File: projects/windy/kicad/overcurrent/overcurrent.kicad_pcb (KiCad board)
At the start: 2 copper layers, 100 x 100 mm, 54 parts, among them J1 USB, J2 USB, J3 USB, J4 USB, K1 VF4_RELAY, P1 SD_CARD, P2 ISP, Q1 PNP, SW1 SWITCHES, U1 ATMEGA328-P, U2 ZXCT1009, U3 LM324, U4 74HC164, U5 DS1307, X1 32k768, Y1 HD44780

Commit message: work in progress
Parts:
- removed the 1PIN at (3.81, 95.9)
- removed the 1PIN at (95.9, 95.9)
- removed the 1PIN at (96.5, 3.81)
- removed the 1PIN at (3.81, 3.81)
- removed J3, J4: USB, conn:USB_A
- removed Y1: HD44780, custom:HD44780
- added 1PIN: P***, conn:1pin, F.Cu at (34.3, 181.6)
- added 1PIN: P***, conn:1pin, F.Cu at (76.2, 181.6)
- added 1PIN: P***, conn:1pin, F.Cu at (127.0, 85.0)
- added 1PIN: P***, conn:1pin, F.Cu at (34.3, 85.0)
- added C7: 0.1u, custom:SM0603_VALUE, F.Cu at (94.2, 185.0)
- added C8: 0.1u, custom:SM0603_VALUE, F.Cu at (90.5, 176.3)
- added D2: DIODE, custom:SOD-323_DIODE, F.Cu at (93.8, 180.0)
- added DS1: HD44780, custom:HD44780, B.Cu at (71.1, 121.9)
- added K2: RELAY_OMRON_G5LE-1, mod:OMNRON G5LE, F.Cu at (71.1, 154.9)
- added Q2: PNP, SMD_Packages:SOT-323, F.Cu at (95.0, 189.1)
- added R17, R18, R19: 51k, custom:SM0603_VALUE, F.Cu at (90.5, 176.3)
- added R20: 1k, custom:SM0603_VALUE, F.Cu at (90.5, 176.3)
- added TB5: 12V, Connect:BARREL_JACK, F.Cu at (41.9, 184.2)
- added TB6: 12V, Connect:BARREL_JACK, F.Cu at (53.3, 184.2)
- C1, C2, C3, C4, C5, R1, R10, R11, R12, R13, R14, R2, R3, R4, R6, R7, R8, R9: footprint cms:SM0805 -> custom:SM0603_VALUE
- C6: value .1u -> 0.1u; footprint cms:SM0805 -> custom:SM0603_VALUE
- D1: footprint discrete:D3 -> custom:SOD-323_DIODE
- K1: value VF4_RELAY -> RELAY_OMRON_G5LE-1; footprint custom:VF4_SOCKET -> mod:OMNRON G5LE
- P1: footprint custom:SD_MMC -> custom:475710001
- Q1: footprint cms:SOT23 -> SMD_Packages:SOT-323
- R15, R16: value 100 -> 51k; footprint cms:SM0805 -> custom:SM0603_VALUE
- SW1: footprint custom:JS5208 -> custom:skrhaae010; moved to B.Cu
- TB1, TB2: footprint custom:TB_2 -> custom:SCREW_TERMINAL_2
- TB3: footprint custom:TB_3 -> custom:SCREW_TERMINAL_3
- U1: moved to B.Cu
- U4: value 74HC164 -> 74LS125
- X1: footprint discrete:QMONTRE -> Crystals_Oscillators_SMD:crystal_FA238-TSX3225
- moved R13 124.3 mm to (114.3, 167.6)
- moved U1 120.7 mm to (71.1, 163.8)
- moved R14 119.4 mm to (114.3, 180.3)
- moved J1 117.9 mm to (114.3, 160.0)
- moved J2 113.7 mm to (113.0, 176.5)
- moved SW1 104.0 mm to (52.1, 163.8), turned to 315 degrees
- moved TB1 98.0 mm to (33.0, 147.3), turned to 270 degrees
- moved K1 97.1 mm to (52.1, 154.9)
- moved TB2 96.8 mm to (33.0, 157.5), turned to 270 degrees
- moved R15 94.6 mm to (90.5, 176.3)
- moved TB3 93.2 mm to (33.0, 170.2), turned to 270 degrees
- moved TB4 92.5 mm to (83.8, 146.1)
- moved R5 90.4 mm to (40.6, 146.1)
- moved BR1 90.4 mm to (40.6, 162.6)
- moved R16 90.4 mm to (90.5, 176.3)
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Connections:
- net /RELAY renamed Net-(Q1-Pad2)
- C6 pad 1: GND -> VCC
- C6 pad 2: VCC -> GND
- J1 pad 1: VCC -> Net-(J1-Pad1)
- J2 pad 1: VCC -> Net-(J1-Pad1)
- P1 pad 2: /SD_CS -> Net-(P1-Pad2)
- P1 pad 5: /SCK -> Net-(P1-Pad5)
- P1 pad 7: /MISO -> Net-(P1-Pad7)
- P2 pad 2: /SCK -> /SCLK
- Q1 pad 1: Net-(Q1-Pad1) -> VCC
- R15 pad 1: Net-(J3-Pad2) -> /SW_L
- R15 pad 2: Net-(J3-Pad3) -> /SW_C
- R16 pad 1: Net-(J4-Pad2) -> /SW_C
- R16 pad 2: Net-(J4-Pad3) -> /SW_U
- RV1 pad 1: GND -> VCC
- RV1 pad 3: VCC -> GND
- SW1 pad 1: GND -> /SW
- U1 pad 10: Net-(U1-Pad10) -> /LCD_BL
- U1 pad 12: /SW_U -> Net-(U1-Pad12)
- U1 pad 13: /SW_D -> Net-(U1-Pad13)
- U1 pad 15: /LCD_E -> Net-(Q2-Pad2)
- U1 pad 19: /SCK -> /SCLK
- U1 pad 2: Net-(U1-Pad2) -> /D4
- U1 pad 21: VCC -> Net-(C8-Pad1)
- U1 pad 26: Net-(U1-Pad26) -> /SW
- U1 pad 3: Net-(U1-Pad3) -> /D5
- U1 pad 4: /SW_C -> /D6
- U1 pad 5: /SW_L -> /D7
- U1 pad 6: /SW_R -> Net-(U1-Pad6)
- U1 pad 9: Net-(U1-Pad9) -> /LCD_E
- U4 pad 1: /MOSI -> GND
- U4 pad 10: Net-(U4-Pad10) -> GND
- U4 pad 11: Net-(U4-Pad11) -> (no net)
- U4 pad 12: Net-(U4-Pad12) -> (no net)
- U4 pad 13: Net-(U4-Pad13) -> (no net)
- U4 pad 14: Net-(U4-Pad14) -> VCC
- U4 pad 2: /MOSI -> /SD_CS
- U4 pad 3: Net-(U4-Pad3) -> Net-(P1-Pad2)
- U4 pad 4: Net-(U4-Pad4) -> GND
- U4 pad 5: Net-(U4-Pad5) -> /SCLK
- U4 pad 6: Net-(U4-Pad6) -> Net-(P1-Pad5)
- U4 pad 7: Net-(U4-Pad7) -> GND
- U4 pad 8: /SCK -> Net-(P1-Pad7)
- U4 pad 9: GND -> /MISO
- VR2 pad 1: /BATTERY -> Net-(K2-Pad3)
- VR2 pad 3: VCC -> Net-(J1-Pad1)
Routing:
- net GND: track 278.4 -> 0.00 mm
- net VCC: track 138.0 -> 0.00 mm
- net /BATTERY: track 91.7 -> 0.00 mm
- net /MOSI: track 54.1 -> 0.00 mm
- net Net-(DS1-Pad3): track 42.4 -> 0.00 mm
- net /Vsense: track 41.7 -> 0.00 mm
- net /DUMMY: track 30.5 -> 0.00 mm
- net /AC1: track 30.1 -> 0.00 mm
- net Net-(C1-Pad2): track 27.6 -> 0.00 mm
- net Net-(C2-Pad2): track 23.3 -> 0.00 mm
- net /RECT: track 22.9 -> 0.00 mm
- net Net-(R8-Pad2): track 14.2 -> 0.00 mm, vias 2 -> 0
- net Net-(C3-Pad1): track 12.9 -> 0.00 mm
- net /ADcurr: track 12.8 -> 0.00 mm
- net Net-(D1-Pad2): track 12.7 -> 0.00 mm
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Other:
- board size 100 x 100 mm -> 100.5 x 103.8 mm

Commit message: starting work on board design
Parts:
- removed 1PIN (x4): P***, conn:1pin
- removed J2: USB, conn:USB_A
- removed K1, K2: RELAY_OMRON_G5LE-1, mod:OMNRON G5LE
- removed RV2: 100, pin:PIN_ARRAY_3X1
- removed TB6: 12V, Connect:BARREL_JACK
- removed VAL: REF, custom:Open_Source_Hardware_Logo
- removed WJ20: VAL**, custom:WJ20
- added C10: 0.1u, custom:SM0603_VALUE, F.Cu at (64.5, 192.0)
- added C11: .1u, custom:SM0603_VALUE, F.Cu at (72.0, 192.5)
- added C12: 470uF, 35V, Discret:C1V5, F.Cu at (118.0, 190.5)
- added C9: 100uF, 35V, Discret:C1V5, F.Cu at (107.0, 189.5)
- added CON1: USB-MINI-B, Connect:USB_Mini-B, F.Cu at (3.00, 142.0)
- added D10: TVS, Housings_SOT-23_SOT-143_TSOT-6:SOT-23, F.Cu at (78.5, 191.0)
- added D3: IN4007, custom:SM0603_DIODE, F.Cu at (58.5, 190.5)
- added D4: LED, LEDs:LED-5MM, F.Cu at (100.0, 136.0)
- added D5: LED, LEDs:LED-5MM, F.Cu at (108.5, 135.5)
- added D6: TVS, Housings_SOT-23_SOT-143_TSOT-6:SOT-23, F.Cu at (100.0, 196.0)
- added D7: TVS, Housings_SOT-23_SOT-143_TSOT-6:SOT-23, F.Cu at (84.5, 190.5)
- added D8: TVS, Housings_SOT-23_SOT-143_TSOT-6:SOT-23, F.Cu at (92.0, 192.5)
- added D9: TVS, Housings_SOT-23_SOT-143_TSOT-6:SOT-23, F.Cu at (82.5, 201.5)
- added F1: FUSE, Fuse_Holders_and_Fuses:BladeFuse-Mini, F.Cu at (46.0, 159.0)
- added F2: FUSE, Fuse_Holders_and_Fuses:BladeFuse-Mini, F.Cu at (46.0, 165.0)
- added P3: ENCODER, Pin_Headers:Pin_Header_Straight_1x05, F.Cu at (127.0, 165.0)
- added Q3: IRF540N, SMD_Packages:DPAK-2, F.Cu at (66.5, 181.0)
- added R21: 100, custom:SM0603_VALUE, F.Cu at (51.0, 192.0)
- added R22: 1k, custom:SM0603_VALUE, F.Cu at (54.5, 188.5)
- added SW2: HWB, custom:sw_42_32, F.Cu at (91.5, 203.5)
- BR1: value RECTIFIER -> FUS45-0045B
- C2, C3: value 1u -> 0.1u
- C4: value 100n -> .1u
- C6, C8: value 0.1u -> .1u
- C7: value 0.1u -> 100uF, 35V; footprint custom:SM0603_VALUE -> Discret:C1V5
- D1: value DIODE -> LED; footprint custom:SOD-323_DIODE -> LEDs:LED-5MM
- D2: value DIODE -> TVS; footprint custom:SOD-323_DIODE -> Housings_SOT-23_SOT-143_TSOT-6:SOT-23
- P1: value SD_CARD -> ISP; footprint custom:475710001 -> custom:ISP_EDGE
- P2: value ISP -> SD_CARD; footprint custom:ISP -> custom:475710001
- Q1, Q2: value PNP -> IRF540N; footprint SMD_Packages:SOT-323 -> SMD_Packages:DPAK-2
- R1: value 2k -> 20k
- R10, R11: value 10k -> 1k
- R13, R14: value 100 -> 10k
- R15: value 51k -> 0.1Ω 1% 5W; footprint custom:SM0603_VALUE -> custom:RESISTOR_POWER
- R16: value 51k -> 10k 1%
- R17: value 51k -> 20k
- R18: value 51k -> 10k
- R19: value 51k -> 1k
- R2: value 1k -> 10k
- R3: value 2k -> 22
- R4: value 1k -> 22
- R5: value .01 9W -> 10k; footprint discrete:TO220_VERT -> custom:SM0603_VALUE
- R6: value 2k -> 1k
- R7: value 40k -> 1k
- R8: value 40k -> 20k
- RV1: footprint pin:PIN_ARRAY_3X1 -> Potentiometers:Potentiometer_WirePads
- SW1: value SWITCHES -> RESET; footprint custom:skrhaae010 -> custom:sw_42_32; moved to F.Cu
- TB1: value DUMMY -> STATOR; footprint custom:SCREW_TERMINAL_2 -> TerminalBlocks:3.5x3
- TB2: value BATTERY -> PVP; footprint custom:SCREW_TERMINAL_2 -> TerminalBlocks:3.5x2
- TB3: value STATOR -> DUMP; footprint custom:SCREW_TERMINAL_3 -> TerminalBlocks:3.5x2
- TB4: value SPST -> BATTERY; footprint pin:pin_array_3x2 -> TerminalBlocks:3.5x2
- TB5: value 12V -> LOAD; footprint Connect:BARREL_JACK -> TerminalBlocks:3.5x2
- U1: value ATMEGA328-P -> LM324; footprint cms:TQFP32 -> Housings_SSOP:TSSOP-14_4.4x5mm_Pitch0.65mm; moved to F.Cu
- U2: value ZXCT1009 -> ATMEGA32U4-A; footprint cms:SOT23 -> Housings_QFP:TQFP-44_10x10mm_Pitch0.8mm
- U3: value LM324 -> INA169; footprint cms:SO14E -> Housings_SOIC:SOIC-8_3.9x4.9mm_Pitch1.27mm
- U4: footprint cms:SO14E -> Housings_SSOP:TSSOP-14_4.4x5mm_Pitch0.65mm
- U5: footprint cms:SO8E -> Housings_SOIC:SOIC-8_3.9x4.9mm_Pitch1.27mm
- VR1, VR2: footprint discrete:TO220_VERT -> SMD_Packages:DPAK-2
- X1: value 32k768 -> 32.768kHz
- moved U1 69.9 mm to (8.89, 195.6)
- moved R5 65.1 mm to (105.5, 151.5)
- moved TB4 52.8 mm to (34.0, 163.5), turned to 270 degrees
- moved U2 49.8 mm to (3.81, 157.5)
- moved SW1 49.3 mm to (3.81, 174.0), turned to 180 degrees
- moved VR1 45.0 mm to (98.0, 162.0)
- moved VR2 44.3 mm to (92.5, 143.0)
- moved R15 42.0 mm to (55.5, 153.0)
- moved Q2 32.5 mm to (66.5, 173.5), turned to 90 degrees
- moved D1 21.5 mm to (91.0, 135.5)
- moved Q1 21.2 mm to (66.5, 166.0)
- moved C7 17.6 mm to (88.0, 168.5)
- moved BR1 17.1 mm to (40.5, 145.5), turned to 90 degrees
- moved TB5 15.8 mm to (34.0, 170.5), turned to 270 degrees
- moved TB3 13.7 mm to (34.0, 156.5)
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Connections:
- net Net-(J1-Pad1) renamed /REGULATED_LOAD
- net Net-(K2-Pad3) renamed /SWITCHED_LOAD
- BR1 pad 1: /RECT -> /SOURCE
- C2 pad 1: /ADcurr -> GND
- C3 pad 1: Net-(C3-Pad1) -> GND
- C3 pad 2: GND -> Net-(C3-Pad2)
- C4 pad 1: GND -> VCC
- C4 pad 2: Net-(C4-Pad2) -> GND
- C7 pad 1: VCC -> /FILTERED_SOURCE
- C8 pad 1: Net-(C8-Pad1) -> VCC
- D1 pad 1: GND -> Net-(D1-Pad1)
- D2 pad 1: GND -> /SOURCE
- D2 pad 2: Net-(D2-Pad2) -> /FUSED_SOURCE
- P1 pad 1: Net-(P1-Pad1) -> /MOSI
- P1 pad 2: Net-(P1-Pad2) -> /SCLK
- P1 pad 3: /MOSI -> /RESET
- P1 pad 5: Net-(P1-Pad5) -> /MOSI
- P2 pad 1: /MOSI -> Net-(P2-Pad1)
- P2 pad 2: /SCLK -> Net-(P2-Pad2)
- P2 pad 3: /RESET -> /MOSI
- P2 pad 5: /MOSI -> Net-(P2-Pad5)
- Q1 pad 1: VCC -> /SOURCE
- Q1 pad 2: Net-(Q1-Pad2) -> Net-(D1-Pad1)
- Q1 pad 3: Net-(D1-Pad2) -> /DUMP_LOAD
- Q2 pad 1: VCC -> /FILTERED_SOURCE
- Q2 pad 2: Net-(Q2-Pad2) -> Net-(D4-Pad1)
- Q2 pad 3: Net-(D2-Pad2) -> /SWITCHED_SOURCE
- R1 pad 1: /BATTERY -> Net-(C1-Pad2)
- R1 pad 2: /ADbatt -> /AC1
- R10 pad 1: /RESET -> Net-(D4-Pad2)
- R10 pad 2: VCC -> GND
- R11 pad 1: /SCL -> Net-(D4-Pad1)
- R11 pad 2: VCC -> /CHARGE_SW
- R12 pad 1: /SDA -> /SCL
- R13 pad 1: Net-(J1-Pad2) -> /SDA
- R13 pad 2: Net-(J1-Pad3) -> VCC
- R14 pad 1: Net-(J2-Pad2) -> Net-(R14-Pad1)
- R14 pad 2: Net-(J2-Pad3) -> VCC
- R15 pad 1: /SW_L -> /BATTERY
- R15 pad 2: /SW_C -> /SWITCHED_SOURCE
- R16 pad 1: /SW_C -> Net-(R16-Pad1)
- R16 pad 2: /SW_U -> GND
- R17 pad 1: /SW_U -> /BATTERY
- R17 pad 2: /SW_R -> /VBATT
- R18 pad 1: /SW_R -> /VBATT
- R18 pad 2: /SW_D -> GND
- R19 pad 1: /SW_D -> Net-(D5-Pad2)
- R2 pad 1: /ADbatt -> Net-(C1-Pad2)
- R20 pad 1: Net-(DS1-Pad15) -> Net-(D5-Pad1)
- R20 pad 2: /LCD_BL -> /LOAD_SW
- R3 pad 1: Net-(C1-Pad2) -> /D+
- R3 pad 2: /AC1 -> Net-(CON1-Pad3)
- R4 pad 1: Net-(C1-Pad2) -> /D-
- R4 pad 2: GND -> Net-(CON1-Pad2)
- R5 pad 1: /Vsense -> VCC
- R5 pad 2: /RECT -> /RESET
- R6 pad 1: Net-(R6-Pad1) -> Net-(D1-Pad2)
- R7 pad 1: Net-(C2-Pad2) -> Net-(D1-Pad1)
- R7 pad 2: Net-(R6-Pad1) -> /DUMP_SW
- R8 pad 1: Net-(C3-Pad1) -> /FILTERED_SOURCE
- R8 pad 2: Net-(R8-Pad2) -> /VIN
- R9 pad 1: Net-(C4-Pad2) -> /VIN
- R9 pad 2: Net-(Q1-Pad2) -> GND
- SW1 pad 1: /SW -> GND
- SW1 pad 2: /SW_L -> /RESET
- TB1 pad 1: /DUMMY -> /AC1
- TB1 pad 2: GND -> /AC2
- TB2 pad 1: /BATTERY -> GND
- TB2 pad 2: GND -> /SOURCE
- TB3 pad 1: /AC1 -> /DUMP_LOAD
- TB3 pad 2: /AC2 -> GND
- TB4 pad 1: Net-(C4-Pad2) -> /BATTERY
- U1 pad 1: /RESET -> /TACH
- U1 pad 10: /LCD_BL -> (no net)
- U1 pad 11: /TACH -> GND
- U1 pad 12: Net-(U1-Pad12) -> (no net)
- U1 pad 13: Net-(U1-Pad13) -> (no net)
- U1 pad 14: Net-(Q1-Pad2) -> (no net)
- U1 pad 2: /D4 -> GND
- U1 pad 3: /D5 -> Net-(C1-Pad2)
- U1 pad 4: /D6 -> VCC
- U1 pad 5: /D7 -> Net-(R16-Pad1)
- U1 pad 6: Net-(U1-Pad6) -> /CURR
- U1 pad 7: VCC -> /CURR
- U1 pad 8: GND -> (no net)
- U1 pad 9: /LCD_E -> (no net)
- U2 pad 1: Net-(R6-Pad1) -> /E6
- U2 pad 2: /RECT -> VCC
- U2 pad 3: /Vsense -> /D-
- U3 pad 1: /TACH -> Net-(R16-Pad1)
- U3 pad 2: Net-(C1-Pad2) -> GND
- U3 pad 3: GND -> /SWITCHED_SOURCE
- U3 pad 4: VCC -> /BATTERY
- U3 pad 5: Net-(C2-Pad2) -> VCC
- U3 pad 6: Net-(R8-Pad2) -> (no net)
- U3 pad 7: Net-(R8-Pad2) -> (no net)
- U3 pad 8: /ADcurr -> (no net)
- U4 pad 3: Net-(P1-Pad2) -> Net-(P2-Pad2)
- U4 pad 6: Net-(P1-Pad5) -> Net-(P2-Pad5)
- U4 pad 8: Net-(P1-Pad7) -> Net-(P2-Pad7)

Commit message: work in progress
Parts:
- F1, F2: footprint Fuse_Holders_and_Fuses:BladeFuse-Mini -> Fuse_Holders_and_Fuses:Fuse_TE5_Littlefuse-395Series
- Q1, Q2, Q3: value IRF540N -> Q_NMOS_GDS
- U3: footprint Housings_SOIC:SOIC-8_3.9x4.9mm_Pitch1.27mm -> Housings_SOT-23_SOT-143_TSOT-6:SOT-23-5
- moved Q1 27.8 mm to (39.5, 159.5), turned to 270 degrees
- moved Q3 27.0 mm to (39.5, 180.0), turned to 270 degrees
- moved R15 14.6 mm to (50.5, 166.8)
- moved F2 8.88 mm to (47.5, 173.8), turned to 180 degrees
- moved F1 5.94 mm to (47.5, 153.2)
- moved Q2 5.80 mm to (60.8, 172.8), turned to 270 degrees
- moved TB1 5.02 mm to (33.5, 144.0)
- moved TB2 5.02 mm to (33.5, 154.5)
- moved TB3 5.02 mm to (33.5, 161.5)
- moved TB4 5.02 mm to (33.5, 168.5)
- moved TB5 5.02 mm to (33.5, 175.5)
- moved BR1 0.25 mm to (40.5, 145.8)
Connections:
- Q1 pad 1: /SOURCE -> Net-(D1-Pad1)
- Q1 pad 2: Net-(D1-Pad1) -> /SOURCE
- Q2 pad 1: /FILTERED_SOURCE -> Net-(D4-Pad1)
- Q2 pad 2: Net-(D4-Pad1) -> /FILTERED_SOURCE
- Q3 pad 1: /FUSED_LOAD -> Net-(D5-Pad1)
- Q3 pad 2: Net-(D5-Pad1) -> /FUSED_LOAD
- TB2 pad 1: GND -> /SOURCE
- TB2 pad 2: /SOURCE -> GND
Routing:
- net /SOURCE: track 0.00 -> 18.6 mm
- net /AC3: track 0.00 -> 7.13 mm
- net /AC1: track 0.00 -> 7.13 mm
- net /AC2: track 0.00 -> 7.00 mm
- net /FUSED_LOAD: track 0.00 -> 6.63 mm
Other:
- net class Power added: clearance 0.254, trace_width 2.54, via_dia 0.889, via_drill 0.635

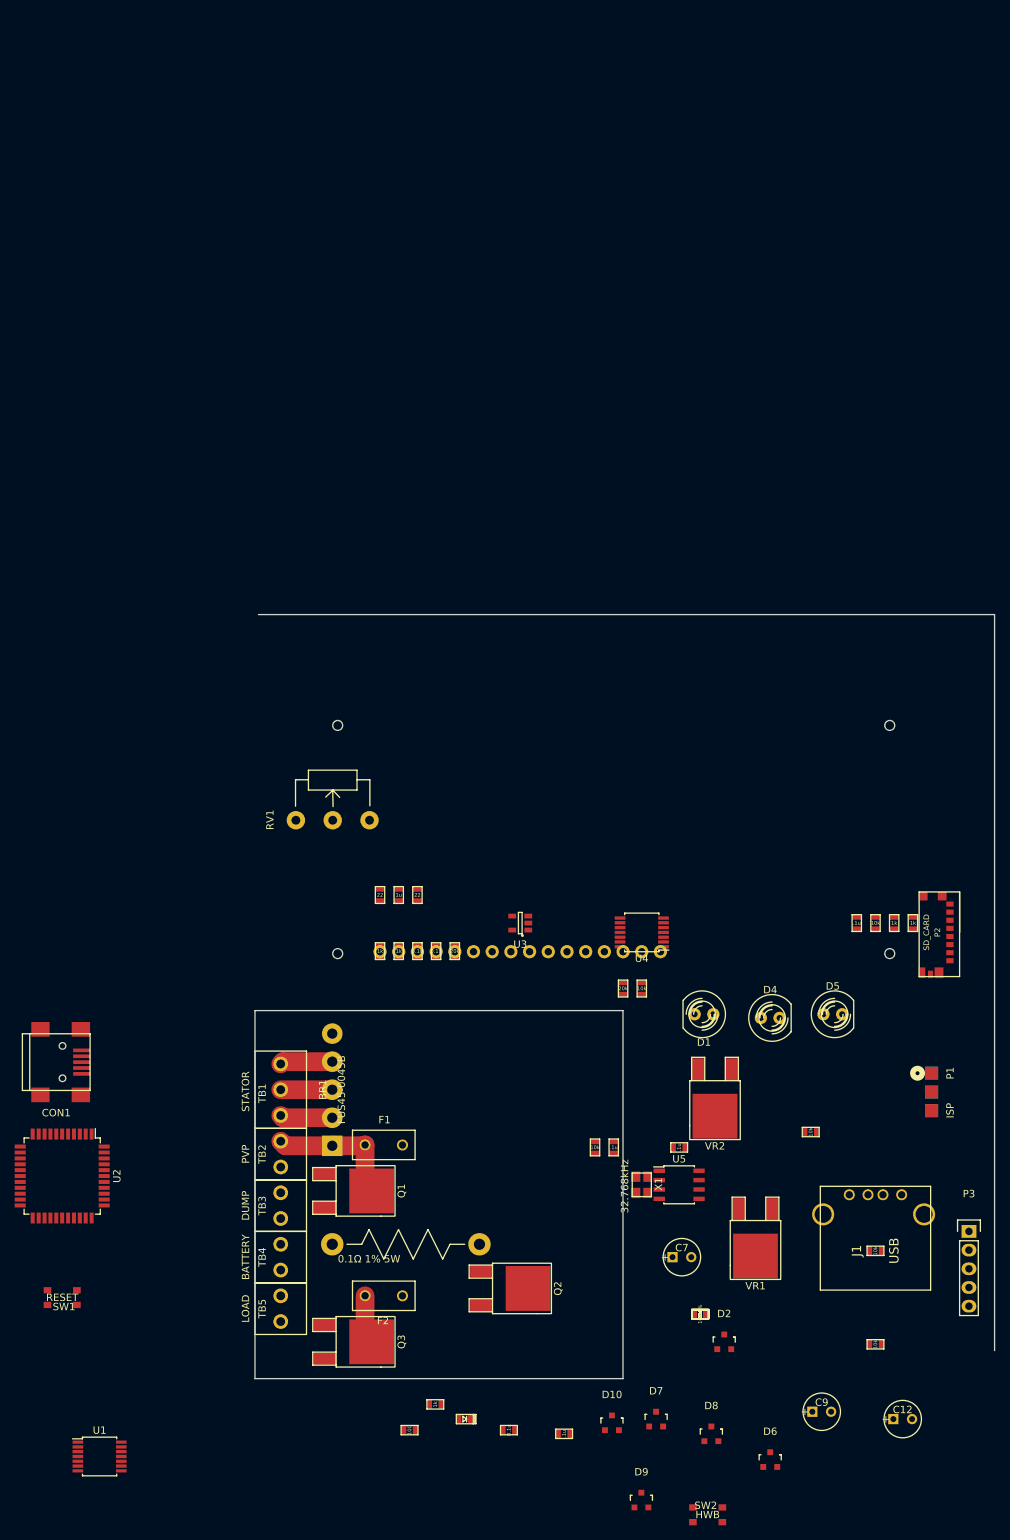
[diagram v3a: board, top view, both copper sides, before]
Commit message: work on board layout; definitely not going to fit in 5x5
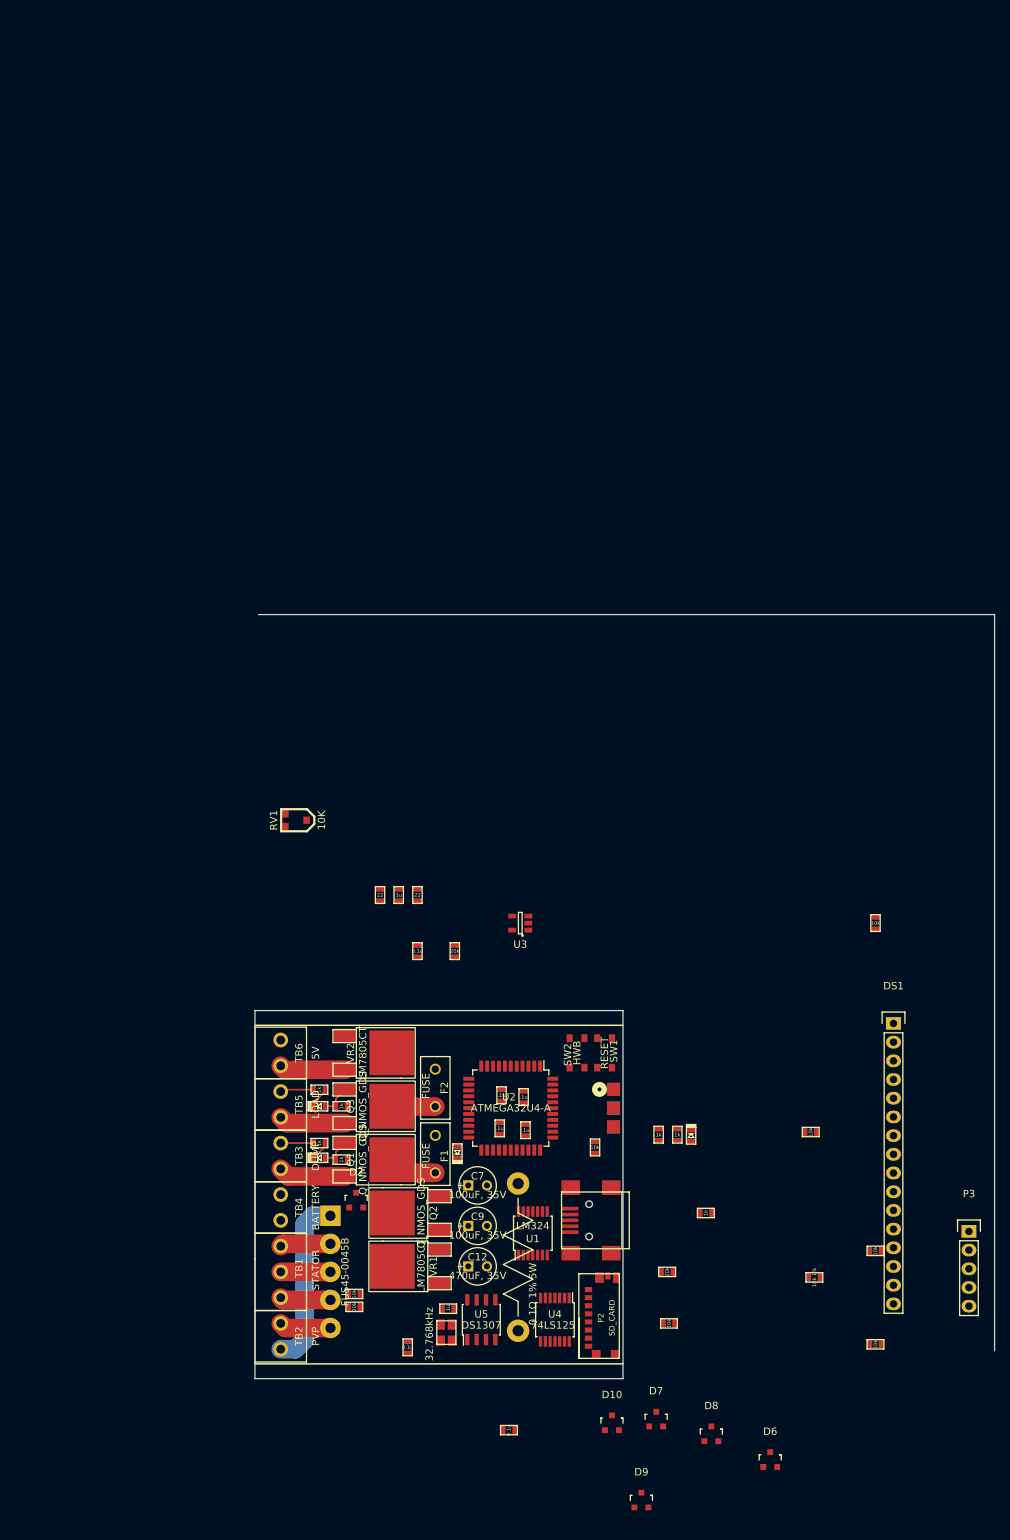
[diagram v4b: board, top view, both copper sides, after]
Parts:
- removed J1: USB, conn:USB_A
- removed R21: 100, custom:SM0603_VALUE
- added TB6: 5V, TerminalBlocks:3.5x2, F.Cu at (33.5, 140.8)
- D1, D4, D5: footprint LEDs:LED-5MM -> custom:SM0603_DIODE
- DS1: footprint custom:HD44780 -> Pin_Headers:Pin_Header_Straight_1x16; moved to F.Cu
- RV1: footprint Potentiometers:Potentiometer_WirePads -> custom:POTENTIOMETER_SMD
- moved SW1 80.8 mm to (77.5, 140.8), turned to 270 degrees
- moved CON1 76.3 mm to (76.2, 163.5), turned to 180 degrees
- moved P2 73.6 mm to (74.0, 176.8), turned to 90 degrees
- moved D5 70.9 mm to (38.8, 148.0), turned to 180 degrees
- moved U1 66.2 mm to (67.8, 165.2), turned to 90 degrees
- moved SW2 65.2 mm to (73.8, 140.8), turned to 90 degrees
- moved U2 61.6 mm to (64.8, 148.2)
- moved C12 61.4 mm to (60.2, 169.8)
- moved R19 60.1 mm to (38.8, 145.8), turned to 180 degrees
- moved R2 57.0 mm to (43.5, 173.5), turned to 0 degrees
- moved R1 56.6 mm to (43.5, 175.2), turned to 180 degrees
- moved R20 56.3 mm to (41.8, 148.0)
- moved D1 55.8 mm to (38.8, 155.0)
- moved C3 54.0 mm to (50.8, 180.8)
- moved U4 53.9 mm to (70.8, 177.0), turned to 270 degrees
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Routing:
- net GND: track 0.00 -> 17.0 mm
- net /SOURCE: track 18.6 -> 30.1 mm
- net /DUMP_LOAD: track 0.00 -> 9.18 mm
- net /SWITCHED_LOAD: track 0.00 -> 9.08 mm
- net /REGULATED_LOAD: track 0.00 -> 7.72 mm
- net Net-(D1-Pad1): track 0.00 -> 4.39 mm
- net Net-(D5-Pad1): track 0.00 -> 4.28 mm
- net Net-(D5-Pad2): track 0.00 -> 2.88 mm
- net Net-(D1-Pad2): track 0.00 -> 2.63 mm
- net /FUSED_LOAD: track 6.63 -> 5.91 mm

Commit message: what am i even doing?
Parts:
- CON1: footprint Connect:USB_Mini-B -> custom:USB_MINI_B_fixed
- D3: footprint custom:SM0603_DIODE -> custom:D2
- moved D6 111.5 mm to (43.8, 99.8), turned to 90 degrees
- moved R18 93.6 mm to (44.0, 94.0), turned to 180 degrees
- moved R17 85.9 mm to (47.0, 94.0), turned to 180 degrees
- moved P3 78.9 mm to (50.5, 145.8), turned to 90 degrees
- moved C12 76.2 mm to (65.2, 93.8)
- moved VR1 76.1 mm to (50.8, 93.8), turned to 270 degrees
- moved R12 73.0 mm to (55.2, 165.9), turned to 180 degrees
- moved RV1 72.2 mm to (72.8, 171.0), turned to 0 degrees
- moved TB4 65.2 mm to (33.5, 96.5)
- moved D8 63.4 mm to (53.0, 142.5)
- moved C1 57.1 mm to (63.5, 174.7)
- moved R16 56.8 mm to (60.0, 138.0), turned to 90 degrees
- moved R14 56.2 mm to (65.5, 152.5), turned to 90 degrees
- moved R13 55.9 mm to (58.4, 165.9)
- moved D2 55.3 mm to (72.0, 113.2), turned to 270 degrees
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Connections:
- net Net-(CON1-Pad1) renamed /VBUS
- D10 pad 1: /D+ -> /D-
- D10 pad 2: /D- -> /D+
- D2 pad 1: /SOURCE -> /FUSED_SOURCE
- D2 pad 2: /FUSED_SOURCE -> /SOURCE
- D9 pad 1: /SCL -> /SDA
- D9 pad 2: /SDA -> /SCL
- P1 pad 1: /MOSI -> /MISO
- P1 pad 2: /SCLK -> VCC
- P1 pad 3: /RESET -> /SCLK
- P1 pad 4: VCC -> /MOSI
- P1 pad 5: /MOSI -> /RESET
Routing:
- net VCC: track 0.00 -> 153.5 mm, vias 0 -> 7
- net /BATTERY: track 0.00 -> 105.6 mm, vias 0 -> 1
- net GND: track 17.0 -> 94.7 mm, vias 0 -> 9
- net /SWITCHED_LOAD: track 9.08 -> 47.6 mm, vias 0 -> 1
- net /MISO: track 0.00 -> 36.8 mm, vias 0 -> 3
- net /MOSI: track 0.00 -> 36.3 mm, vias 0 -> 2
- net /D7: track 0.00 -> 32.7 mm
- net /D5: track 0.00 -> 32.6 mm, vias 0 -> 1
- net Net-(DS1-Pad15): track 0.00 -> 31.5 mm
- net /D6: track 0.00 -> 31.0 mm
- net /SCLK: track 0.00 -> 30.3 mm
- net /VBUS: track 0.00 -> 27.0 mm, vias 0 -> 2
- net /D4: track 0.00 -> 26.5 mm
- net /SWITCHED_SOURCE: track 0.00 -> 25.0 mm
- net /SOURCE: track 30.1 -> 53.1 mm
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- added copper zone on B.Cu, net GND
- added copper zone on F.Cu, net GND
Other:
- board size 100.5 x 103.8 mm -> 50 x 100 mm
- net class Default: clearance 0.254 -> 0.1778
- net class VCC added: clearance 0.1778, trace_width 0.381, via_dia 0.889, via_drill 0.635
- rule trace_clearance: 0.254 -> 0.1778
